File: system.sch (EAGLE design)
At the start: 61 parts, among them IC1 TPS7B8650BQDDARQ1, IC2 TLV9101IDBVR, IC3 TLV9101IDBVR, J1 TSW-104-07-F-S, J2 163-179PH-EX, J3 RS1-02-G, SW1 1825910-6, SW2 1825910-6, SW3 1825910-6, U1 ATMEGA328PB-AU

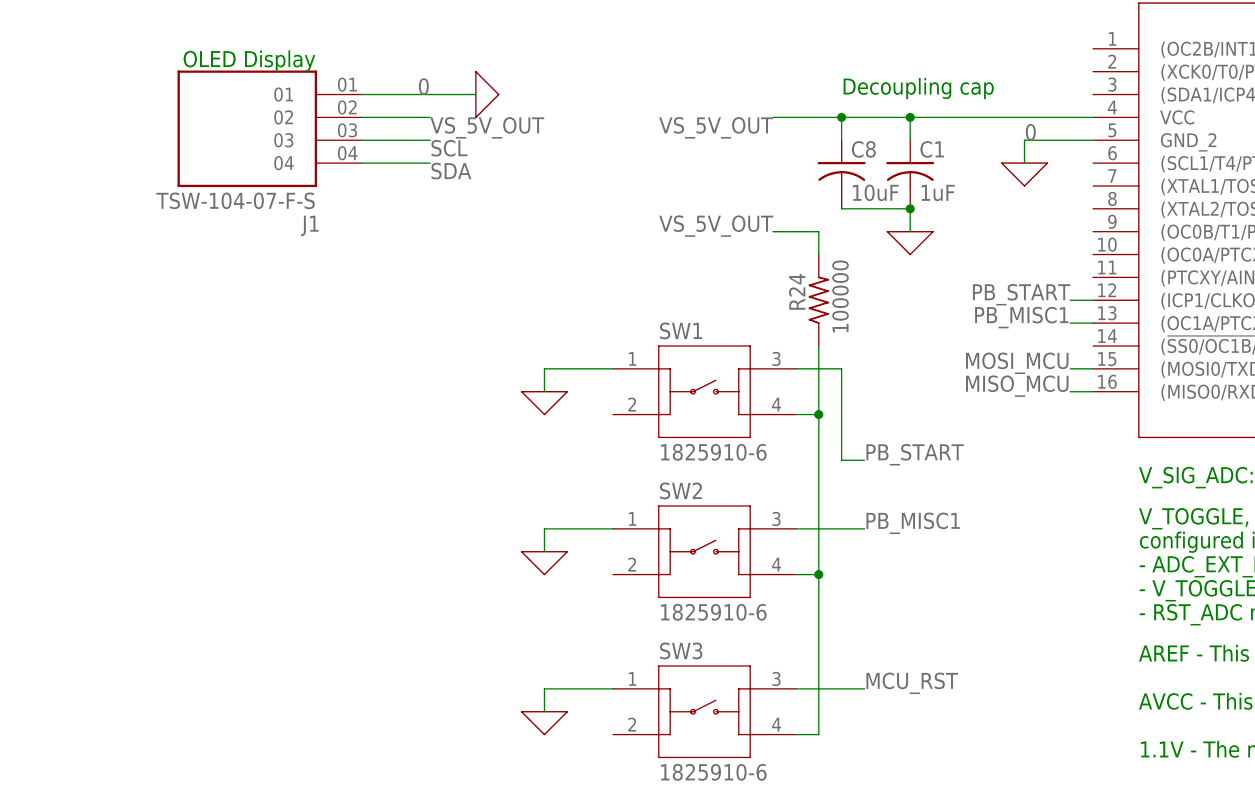
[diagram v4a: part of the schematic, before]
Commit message: Added EXT CLK
Added an external clock of 16MHz to MCU
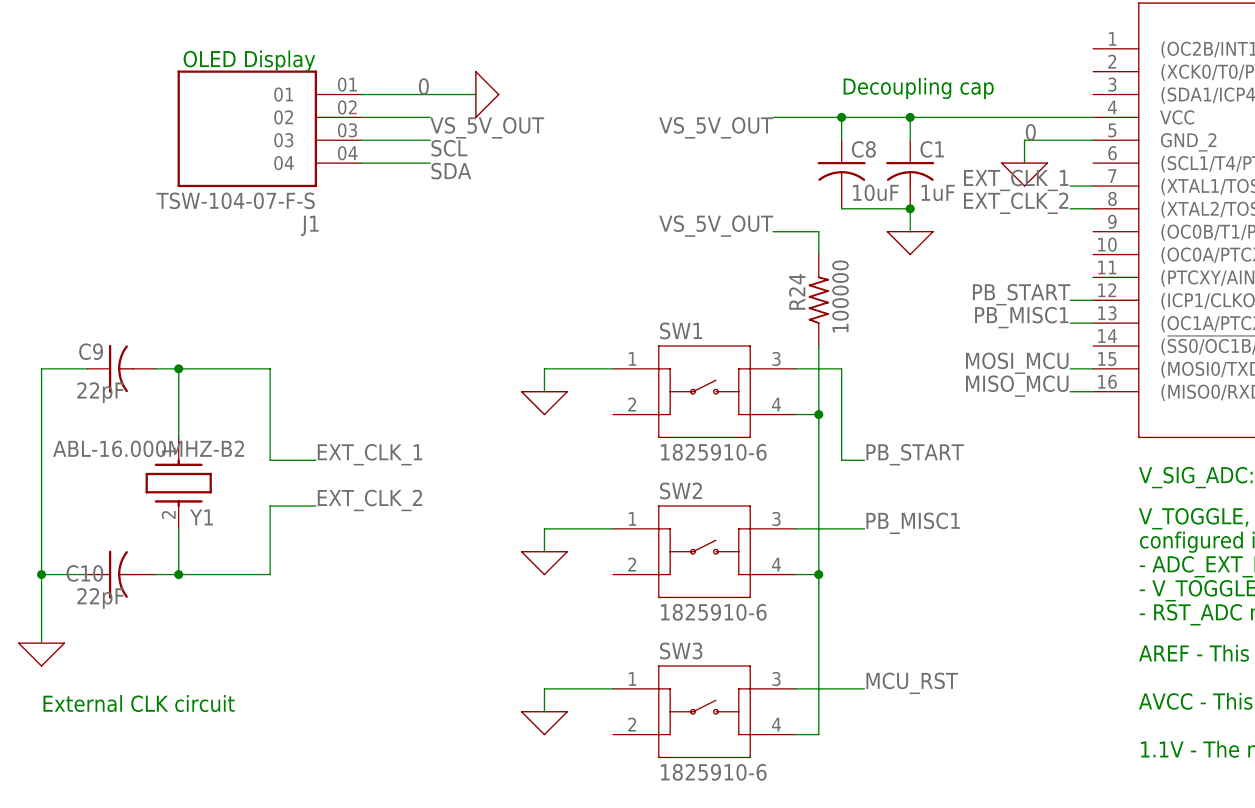
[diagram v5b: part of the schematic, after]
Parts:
- added C10, C9: 22pF, rcl:C-USC0603
- added Y1: ABL-16.000MHZ-B2, ABL-16.000MHZ-B2:ABL-16.000MHZ-B2
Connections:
- new net EXT_CLK_1: C9.2, U1.(XTAL1/TOSC1)PB6, Y1.1
- new net EXT_CLK_2: C10.2, U1.(XTAL2/TOSC2)PB7, Y1.2
- net 0: now also C10.1, C9.1
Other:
- note added: "External CLK circuit"
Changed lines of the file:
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@@
 <part name="X_27" library="ngspice-simulation" library_urn="urn:adsk.eagle:library:527439" deviceset="GND" device=""/>
 <part name="X_28" library="ngspice-simulation" library_urn="urn:adsk.eagle:library:527439" deviceset="GND" device=""/>
+<part name="Y1" library="ABL-16.000MHZ-B2" deviceset="ABL-16.000MHZ-B2" device=""/>
+<part name="X_29" library="ngspice-simulation" library_urn="urn:adsk.eagle:library:527439" deviceset="GND" device=""/>
+<part name="C9" library="rcl" library_urn="urn:adsk.eagle:library:334" deviceset="C-US" device="C0603" package3d_urn="urn:adsk.eagle:package:23616/2" value="22pF"/>
+<part name="C10" library="rcl" library_urn="urn:adsk.eagle:library:334" deviceset="C-US" device="C0603" package3d_urn="urn:adsk.eagle:package:23616/2" value="22pF"/>
 </parts>
 <sheets>
@@
 <text x="-325.12" y="-43.18" size="1.778" layer="91">Programming pins for MCU</text>
 <text x="-195.58" y="10.16" size="1.778" layer="91">Testpoints</text>
+<text x="-388.62" y="-139.7" size="1.778" layer="91">External CLK circuit</text>
 </plain>
 <moduleinsts>
@@
 <instance part="X_27" gate="G$1" x="2.54" y="-33.02" smashed="yes"/>
 <instance part="X_28" gate="G$1" x="-7.62" y="-109.22" smashed="yes"/>
+<instance part="Y1" gate="G$1" x="-373.38" y="-109.22" smashed="yes" rot="R270">
+<attribute name="NAME" x="-372.11" y="-118.11" size="1.778" layer="95" align="center-left"/>
+<attribute name="VALUE" x="-387.35" y="-110.49" size="1.778" layer="96" align="center-left"/>
+</instance>
+<instance part="X_29" gate="G$1" x="-388.62" y="-132.08" smashed="yes"/>
+<instance part="C9" gate="G$1" x="-381" y="-101.6" smashed="yes" rot="R90">
+<attribute name="NAME" x="-381.635" y="-100.584" size="1.778" layer="95" rot="MR0"/>
+<attribute name="VALUE" x="-379.349" y="-103.124" size="1.778" layer="96" rot="R180"/>
+</instance>
+<instance part="C10" gate="G$1" x="-381" y="-124.46" smashed="yes" rot="R90">
+<attribute name="NAME" x="-381.635" y="-123.444" size="1.778" layer="95" rot="R180"/>
+<attribute name="VALUE" x="-379.349" y="-125.984" size="1.778" layer="96" rot="R180"/>
+</instance>
 </instances>
 <busses>
@@
 <wire x1="-332.74" y1="-137.16" x2="-332.74" y2="-139.7" width="0.1524" layer="91"/>
 </segment>
-</net>
+<segment>
+<pinref part="X_29" gate="G$1" pin="0"/>
+<wire x1="-388.62" y1="-132.08" x2="-388.62" y2="-124.46" width="0.1524" layer="91"/>
+<pinref part="C9" gate="G$1" pin="1"/>
+<wire x1="-388.62" y1="-124.46" x2="-388.62" y2="-101.6" width="0.1524" layer="91"/>
+<wire x1="-388.62" y1="-101.6" x2="-383.54" y2="-101.6" width="0.1524" layer="91"/>
+<pinref part="C10" gate="G$1" pin="1"/>
+<wire x1="-383.54" y1="-124.46" x2="-388.62" y2="-124.46" width="0.1524" layer="91"/>
+<junction x="-388.62" y="-124.46"/>
+</segment>
+</net>
+<net name="EXT_CLK_1" class="0">
+<segment>
+<pinref part="C9" gate="G$1" pin="2"/>
+<wire x1="-375.92" y1="-101.6" x2="-373.38" y2="-101.6" width="0.1524" layer="91"/>
+<pinref part="Y1" gate="G$1" pin="1"/>
+<wire x1="-373.38" y1="-101.6" x2="-373.38" y2="-109.22" width="0.1524" layer="91"/>
+<wire x1="-373.38" y1="-101.6" x2="-363.22" y2="-101.6" width="0.1524" layer="91"/>
+<junction x="-373.38" y="-101.6"/>
+<wire x1="-363.22" y1="-101.6" x2="-363.22" y2="-111.76" width="0.1524" layer="91"/>
+<wire x1="-363.22" y1="-111.76" x2="-358.14" y2="-111.76" width="0.1524" layer="91"/>
+<label x="-358.14" y="-111.76" size="1.778" layer="95"/>
+</segment>
+<segment>
+<pinref part="U1" gate="A" pin="(XTAL1/TOSC1)PB6"/>
+<wire x1="-271.78" y1="-81.28" x2="-274.32" y2="-81.28" width="0.1524" layer="91"/>
+<label x="-274.32" y="-81.28" size="1.778" layer="95" rot="MR0"/>
+</segment>
+</net>
+<net name="EXT_CLK_2" class="0">
+<segment>
+<pinref part="Y1" gate="G$1" pin="2"/>
+<wire x1="-373.38" y1="-119.38" x2="-373.38" y2="-124.46" width="0.1524" layer="91"/>
+<pinref part="C10" gate="G$1" pin="2"/>
+<wire x1="-373.38" y1="-124.46" x2="-375.92" y2="-124.46" width="0.1524" layer="91"/>
+<wire x1="-373.38" y1="-124.46" x2="-363.22" y2="-124.46" width="0.1524" layer="91"/>
+<junction x="-373.38" y="-124.46"/>
+<wire x1="-363.22" y1="-124.46" x2="-363.22" y2="-116.84" width="0.1524" layer="91"/>
+<wire x1="-363.22" y1="-116.84" x2="-358.14" y2="-116.84" width="0.1524" layer="91"/>
+<label x="-358.14" y="-116.84" size="1.778" layer="95"/>
+</segment>
+<segment>
+<pinref part="U1" gate="A" pin="(XTAL2/TOSC2)PB7"/>
+<wire x1="-271.78" y1="-83.82" x2="-274.32" y2="-83.82" width="0.1524" layer="91"/>
+<label x="-274.32" y="-83.82" size="1.778" layer="95" rot="MR0"/>
+</segment>
+</net>

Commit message: added caps
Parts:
- added C11, C12, C13: 1uF, rcl:C-USC0603
- R24: value 100000 -> 100k
- R7, R8: value 2000000 -> 2M
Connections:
- net 0: now also C11.2, C12.2, C13.2
- net VS_1.5V_OUT: now also C13.1
- net VS_2.5V_OUT: now also C12.1
- net VS_5V_OUT: now also C11.1
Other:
- moved on the sheet: R10, R11, R9

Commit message: update some stuff
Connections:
- net VS_1.5V: no longer C3.1
- net VS_2.5V: no longer C5.1
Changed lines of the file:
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@@
 <part name="X_9" library="ngspice-simulation" library_urn="urn:adsk.eagle:library:527439" deviceset="GND" device=""/>
 <part name="IC3" library="TLV9101IDBVR" deviceset="TLV9101IDBVR" device=""/>
-<part name="C3" library="rcl" library_urn="urn:adsk.eagle:library:334" deviceset="C-US" device="C0603" package3d_urn="urn:adsk.eagle:package:23616/2" value="1uF"/>
 <part name="R5" library="rcl" library_urn="urn:adsk.eagle:library:334" deviceset="R-US_" device="R0603" package3d_urn="urn:adsk.eagle:package:23555/3" value="560k"/>
 <part name="R6" library="rcl" library_urn="urn:adsk.eagle:library:334" deviceset="R-US_" device="R0603" package3d_urn="urn:adsk.eagle:package:23555/3" value="240k"/>
 <part name="X_10" library="ngspice-simulation" library_urn="urn:adsk.eagle:library:527439" deviceset="GND" device=""/>
-<part name="X_11" library="ngspice-simulation" library_urn="urn:adsk.eagle:library:527439" deviceset="GND" device=""/>
 <part name="X_12" library="ngspice-simulation" library_urn="urn:adsk.eagle:library:527439" deviceset="GND" device=""/>
 <part name="C4" library="rcl" library_urn="urn:adsk.eagle:library:334" deviceset="C-US" device="C0603" package3d_urn="urn:adsk.eagle:package:23616/2" value="1uF"/>
 <part name="R7" library="rcl" library_urn="urn:adsk.eagle:library:334" deviceset="R-US_" device="R0603" package3d_urn="urn:adsk.eagle:package:23555/3" value="0"/>
 <part name="R8" library="rcl" library_urn="urn:adsk.eagle:library:334" deviceset="R-US_" device="R0603" package3d_urn="urn:adsk.eagle:package:23555/3" value="0"/>
-<part name="C5" library="rcl" library_urn="urn:adsk.eagle:library:334" deviceset="C-US" device="C0603" package3d_urn="urn:adsk.eagle:package:23616/2" value="1uF"/>
-<part name="X_7" library="ngspice-simulation" library_urn="urn:adsk.eagle:library:527439" deviceset="GND" device=""/>
 </parts>
 <sheets>
@@
 <attribute name="VALUE" x="64.008" y="-1.27" size="1.778" layer="96" align="center-left"/>
 </instance>
-<instance part="C3" gate="G$1" x="91.44" y="-15.24" smashed="yes">
-<attribute name="NAME" x="92.456" y="-14.605" size="1.778" layer="95"/>
-<attribute name="VALUE" x="92.456" y="-19.431" size="1.778" layer="96"/>
-</instance>
 <instance part="R5" gate="G$1" x="33.02" y="-2.54" smashed="yes" rot="R270">
 <attribute name="NAME" x="34.5186" y="1.27" size="1.778" layer="95" rot="R270"/>
@@
 </instance>
 <instance part="X_10" gate="G$1" x="55.88" y="-12.7" smashed="yes"/>
-<instance part="X_11" gate="G$1" x="91.44" y="-22.86" smashed="yes"/>
 <instance part="X_12" gate="G$1" x="33.02" y="-25.4" smashed="yes"/>
 <instance part="C4" gate="G$1" x="-22.86" y="49.276" smashed="yes">
@@
 <attribute name="VALUE" x="2.794" y="27.178" size="1.778" layer="96"/>
 </instance>
-<instance part="C5" gate="G$1" x="106.68" y="60.96" smashed="yes">
-<attribute name="NAME" x="107.696" y="61.595" size="1.778" layer="95"/>
-<attribute name="VALUE" x="107.696" y="56.769" size="1.778" layer="96"/>
-</instance>
-<instance part="X_7" gate="G$1" x="106.68" y="50.8" smashed="yes"/>
 </instances>
 <busses>
@@
 <pinref part="IC2" gate="G$1" pin="IN-"/>
 <wire x1="104.14" y1="68.58" x2="101.6" y2="68.58" width="0.1524" layer="91"/>
-<wire x1="104.14" y1="68.58" x2="106.68" y2="68.58" width="0.1524" layer="91"/>
 <junction x="104.14" y="68.58"/>
 <label x="109.22" y="68.58" size="1.778" layer="95"/>
-<pinref part="C5" gate="G$1" pin="1"/>
-<wire x1="106.68" y1="68.58" x2="109.22" y2="68.58" width="0.1524" layer="91"/>
-<wire x1="106.68" y1="63.5" x2="106.68" y2="68.58" width="0.1524" layer="91"/>
-<junction x="106.68" y="68.58"/>
+<wire x1="104.14" y1="68.58" x2="109.22" y2="68.58" width="0.1524" layer="91"/>
 </segment>
 <segment>
@@
 <pinref part="IC3" gate="G$1" pin="IN-"/>
 <wire x1="83.82" y1="-5.08" x2="86.36" y2="-5.08" width="0.1524" layer="91"/>
-<wire x1="93.98" y1="-5.08" x2="91.44" y2="-5.08" width="0.1524" layer="91"/>
 <pinref part="IC3" gate="G$1" pin="OUT"/>
-<wire x1="91.44" y1="-5.08" x2="86.36" y2="-5.08" width="0.1524" layer="91"/>
+<wire x1="93.98" y1="-5.08" x2="86.36" y2="-5.08" width="0.1524" layer="91"/>
 <wire x1="58.42" y1="-5.08" x2="50.8" y2="-5.08" width="0.1524" layer="91"/>
 <wire x1="50.8" y1="-5.08" x2="50.8" y2="5.08" width="0.1524" layer="91"/>
@@
 <wire x1="86.36" y1="5.08" x2="86.36" y2="-5.08" width="0.1524" layer="91"/>
 <junction x="86.36" y="-5.08"/>
-<pinref part="C3" gate="G$1" pin="1"/>
-<wire x1="91.44" y1="-5.08" x2="91.44" y2="-12.7" width="0.1524" layer="91"/>
-<junction x="91.44" y="-5.08"/>
 <label x="93.98" y="-5.08" size="1.778" layer="95"/>
 </segment>
@@
 <net name="0" class="0">
 <segment>
-<pinref part="C5" gate="G$1" pin="2"/>
-<wire x1="106.68" y1="55.88" x2="106.68" y2="50.8" width="0.1524" layer="91"/>
-<pinref part="X_7" gate="G$1" pin="0"/>
-</segment>
-<segment>
 <pinref part="IC3" gate="G$1" pin="V-"/>
 <wire x1="58.42" y1="-7.62" x2="55.88" y2="-7.62" width="0.1524" layer="91"/>
@@
 </segment>
 <segment>
-<pinref part="C3" gate="G$1" pin="2"/>
-<wire x1="91.44" y1="-20.32" x2="91.44" y2="-22.86" width="0.1524" layer="91"/>
-<pinref part="X_11" gate="G$1" pin="0"/>
-</segment>
-<segment>
